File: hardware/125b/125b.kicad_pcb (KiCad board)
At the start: 2 copper layers, 59 x 75 mm, 49 parts, among them J1 Guitar in, J2 Barrel_Jack, J3 Conn_02x05_Odd_Even_MountingP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, J4 Guitar out, SW1 SW_Push_SPDT, SW2 RotaryEncoder_Switch, SW3 SW_Push, SW4 SW_Push, U1 L78L05_TO92, U2 TL074

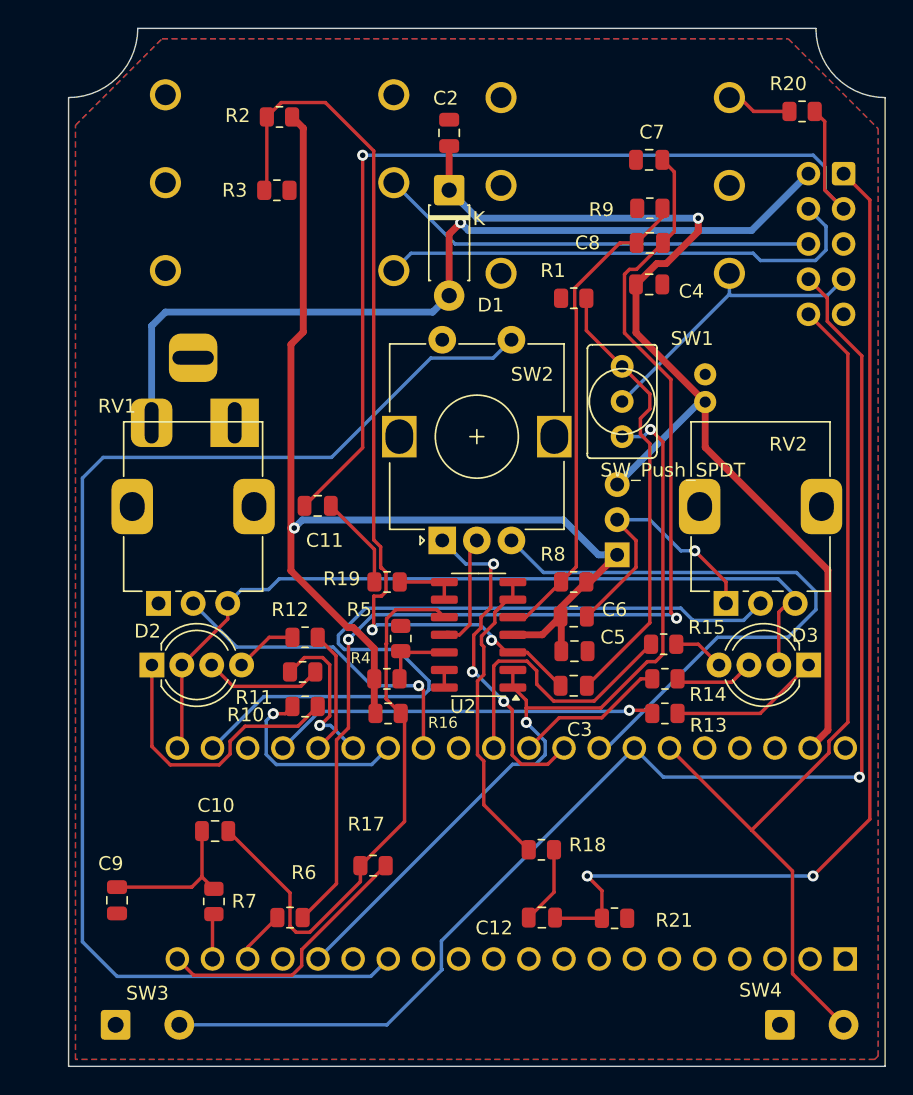
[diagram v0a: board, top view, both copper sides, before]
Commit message: Thinner neutrik audio sockets
ALlows power socket to move to back of board again
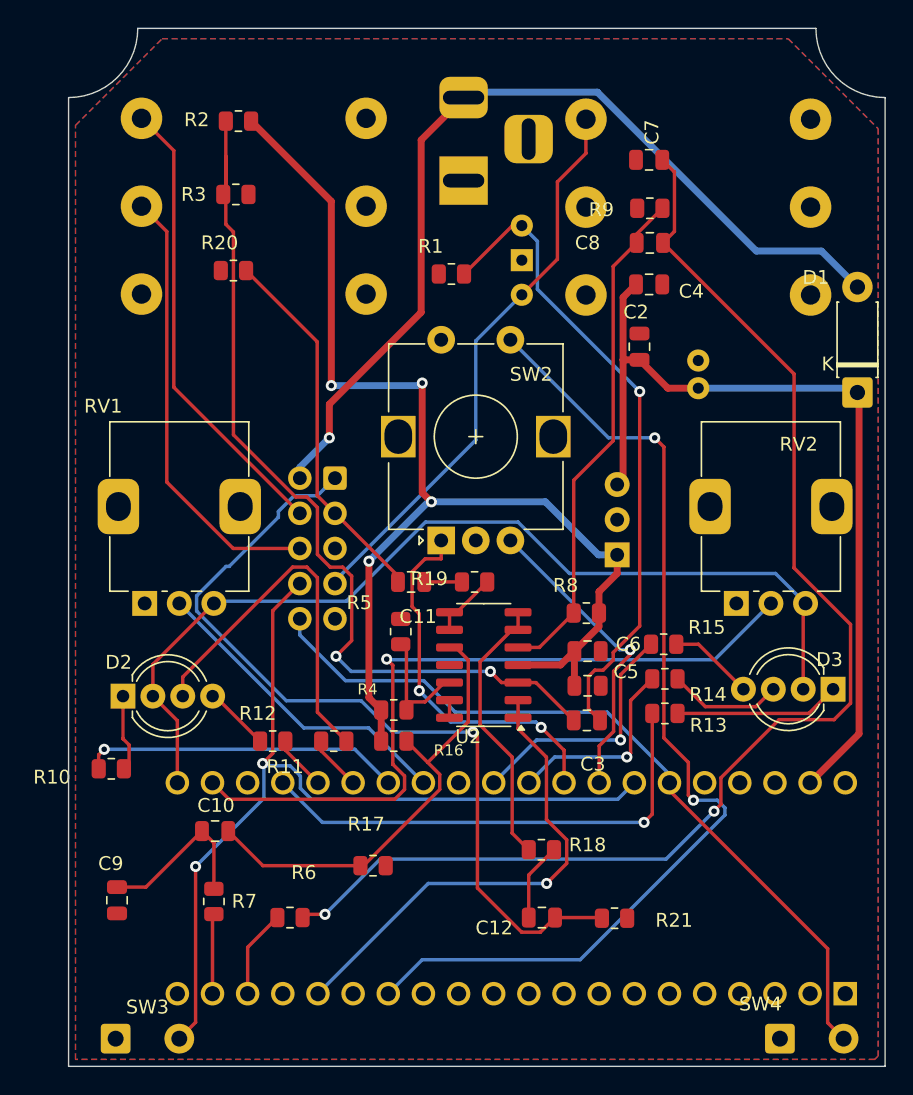
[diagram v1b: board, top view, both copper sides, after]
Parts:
- J1, J4: footprint Project:NYS215 -> Project:Jack_6.35mm_Neutrik_NMJ6HCD2_Horizontal
- SW1: footprint PCM_4ms_Switch:Switch_Toggle_SPDT_SubMini -> Project:mini_switch_jaycar_SPDT; moved to B.Cu
- moved J3 42.8 mm to (117.2, 67.5)
- moved R20 42.7 mm to (109.9, 52.5)
- moved D1 32.9 mm to (155.0, 61.3), turned to 90 degrees
- moved J2 24.1 mm to (126.5, 46.0), turned to -90 degrees
- moved C2 20.7 mm to (139.2, 58.0)
- moved R10 14.7 mm to (101.1, 88.5)
- moved J1 12.7 mm to (135.4, 41.6), turned to -90 degrees
- moved J4 11.1 mm to (103.3, 41.5), turned to -90 degrees
- moved SW1 9.56 mm to (132.3, 54.2), turned to 90 degrees
- moved R1 9.01 mm to (125.7, 52.8)
- moved C11 8.71 mm to (122.8, 75.0)
- moved R12 7.86 mm to (112.8, 86.5)
- moved R19 6.33 mm to (127.3, 75.0)
- moved R11 5.48 mm to (117.2, 86.5)
- moved D2 3.07 mm to (101.9, 83.2)
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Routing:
- net GND: track 53.1 -> 0.00 mm, vias 1 -> 0
- net /fsw3: track 72.3 -> 27.1 mm, vias 1 -> 0
- net /fsw8: track 97.2 -> 65.3 mm, vias 1 -> 2
- net /Left in: track 60.0 -> 35.1 mm, vias 2 -> 1
- net /ENC_B: track 44.6 -> 22.5 mm, vias 0 -> 1
- net /fsw7: track 21.2 -> 41.1 mm
- net /ENC_CLICK: track 92.3 -> 73.4 mm, vias 0 -> 2
- net Net-(D2-GK): track 8.55 -> 27.4 mm
- net /fsw1: track 76.4 -> 60.6 mm, vias 2 -> 1
- net /VCC: track 78.3 -> 62.6 mm, vias 1 -> 0
- net Net-(D2-RK): track 20.7 -> 5.59 mm
- net Net-(SW1-A): track 32.3 -> 47.1 mm, vias 0 -> 1
- net /fsw10: track 66.5 -> 56.4 mm
- net /3v3: track 59.5 -> 69.4 mm
- net Net-(C7-Pad2): track 82.9 -> 92.7 mm
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
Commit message: Get everything connected
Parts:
- moved C5 6.25 mm to (137.2, 76.5), turned to 90 degrees
- moved R8 1.00 mm to (134.8, 76.5), turned to 90 degrees
- moved SW3 0.74 mm to (100.7, 107.8)
- moved R3 0.64 mm to (109.5, 46.8), turned to 180 degrees
- moved SW4 0.25 mm to (149.4, 107.8)
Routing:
- net GND: track 0.00 -> 37.9 mm
- net Net-(U2B-+): track 37.0 -> 41.3 mm
- net Net-(U2A-+): track 65.8 -> 63.4 mm
- net /fsw3: track 27.1 -> 28.2 mm
- net +5V: track 86.9 -> 85.7 mm
- net Net-(SW1-A): track 47.1 -> 48.0 mm

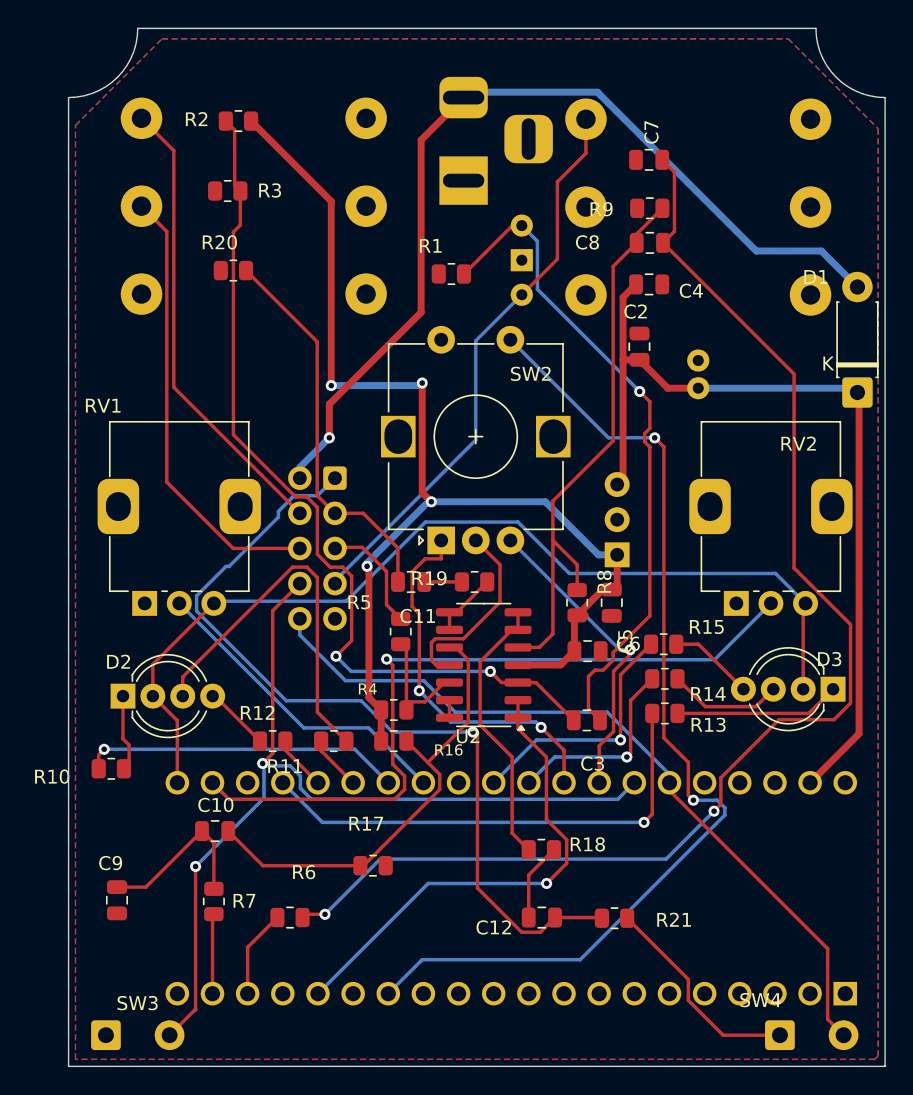
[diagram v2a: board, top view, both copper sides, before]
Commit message: Tiday up references on board and move c1
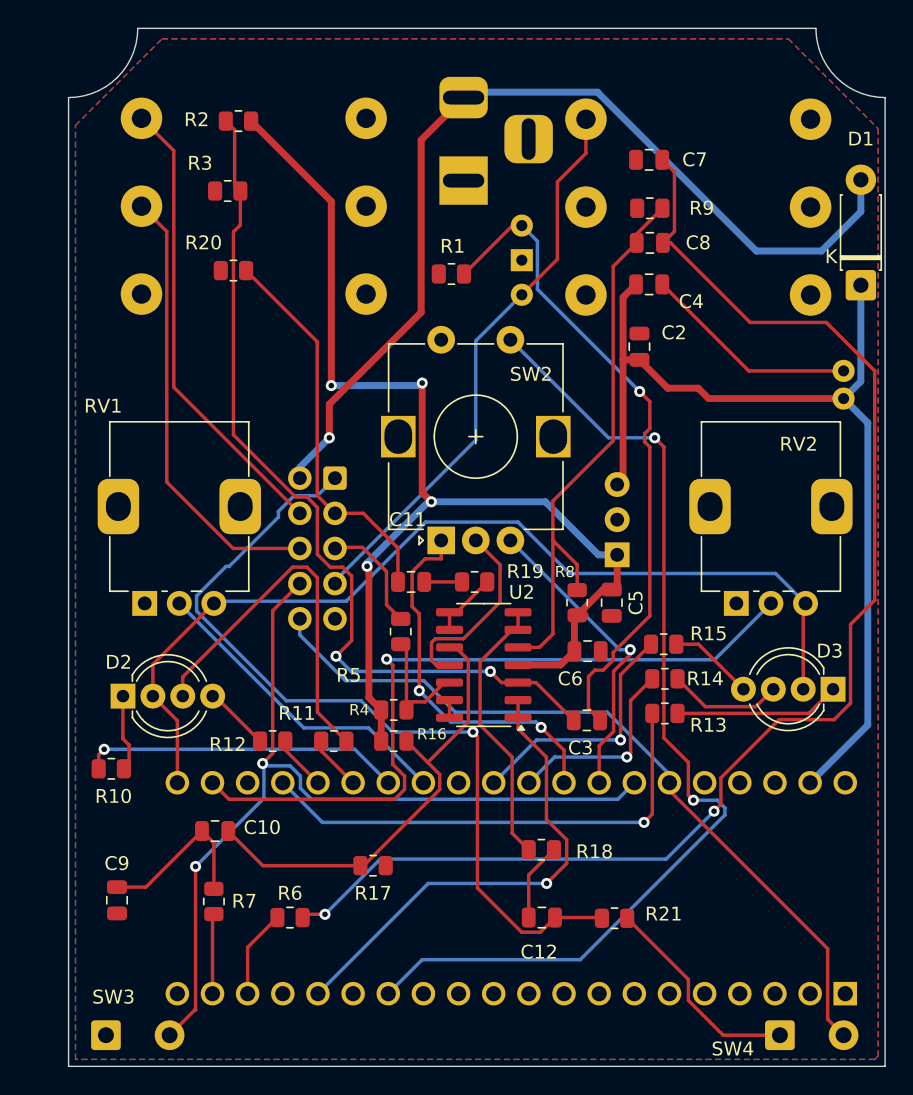
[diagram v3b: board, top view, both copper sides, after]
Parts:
- moved C1 10.5 mm to (154.0, 61.8)
- moved D1 7.75 mm to (155.2, 53.6)
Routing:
- net GND: track 37.9 -> 53.6 mm
- net /VCC: track 62.6 -> 71.0 mm
- net Net-(C7-Pad2): track 92.7 -> 97.7 mm
- net /fsw2: track 66.9 -> 69.5 mm

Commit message: Trace and component adjustments
Also add local footprints
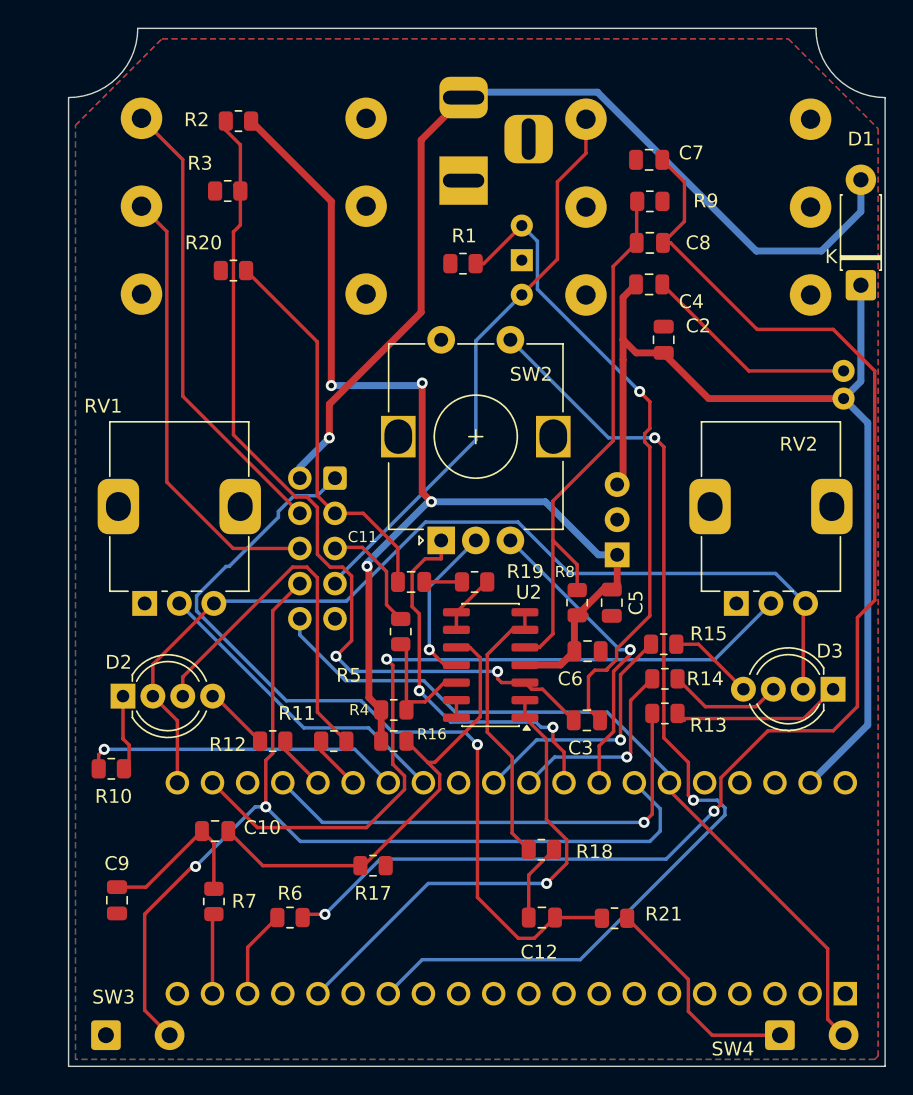
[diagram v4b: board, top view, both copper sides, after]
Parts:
- moved C2 1.82 mm to (141.0, 57.5)
- moved R1 1.12 mm to (126.5, 52.0)
- moved R9 0.50 mm to (140.0, 47.5), turned to 0 degrees
- moved U2 0.50 mm to (128.5, 81.0)
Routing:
- net /fsw8: track 65.4 -> 72.8 mm
- net GND: track 53.6 -> 51.7 mm, vias 0 -> 1
- net Net-(A1-ADC_0): track 54.1 -> 55.8 mm
- net Net-(U2C-+): track 33.4 -> 35.0 mm
- net Net-(C7-Pad2): track 97.7 -> 98.7 mm
- net Net-(D3-RK): track 12.0 -> 13.0 mm
- net Net-(U2A-+): track 63.4 -> 64.3 mm
- net Net-(U2B-+): track 41.3 -> 40.5 mm
- net /VCC: track 71.0 -> 71.7 mm
- net /ENC_A: track 27.2 -> 27.7 mm
- net +5V: track 85.7 -> 85.2 mm
